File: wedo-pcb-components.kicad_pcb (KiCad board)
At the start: 2 copper layers, 1 part, among them U1 TPS61032

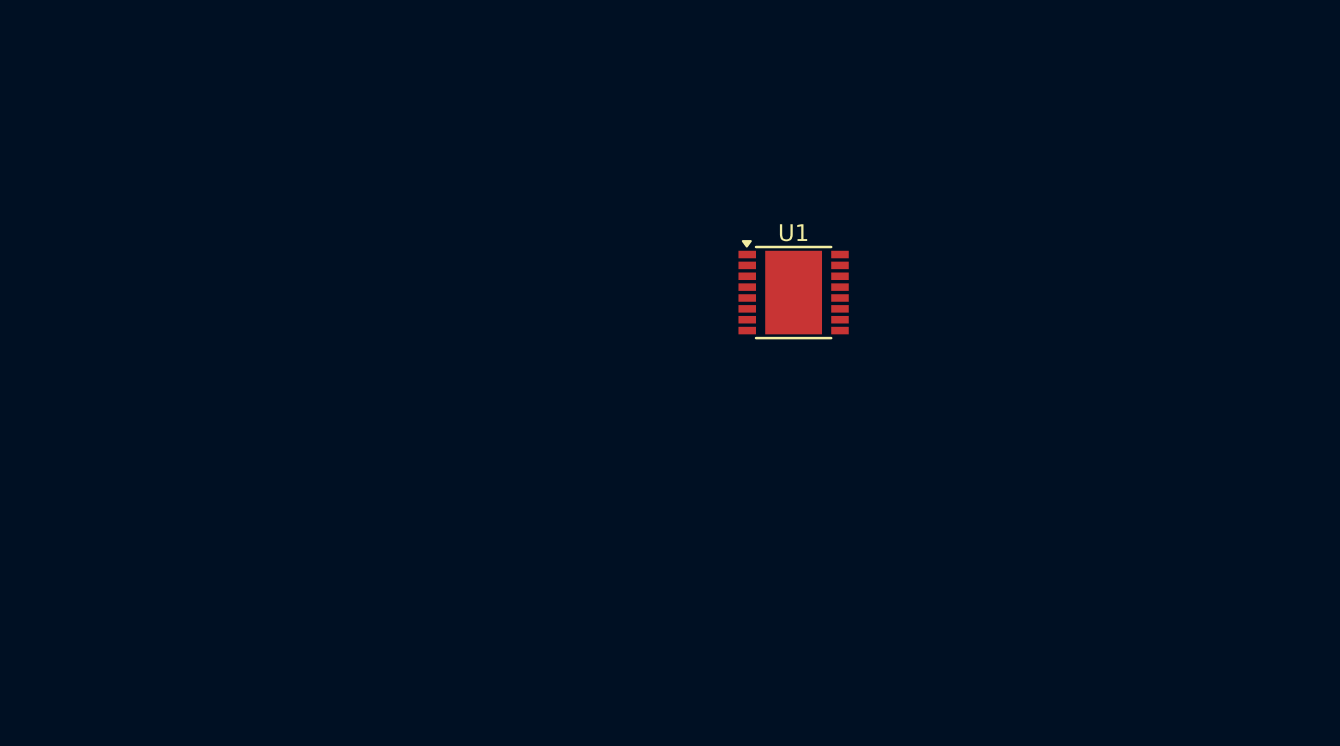
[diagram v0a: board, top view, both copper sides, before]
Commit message: Add 6p6c connector footprint and adjust PCB geometry with mounting holes
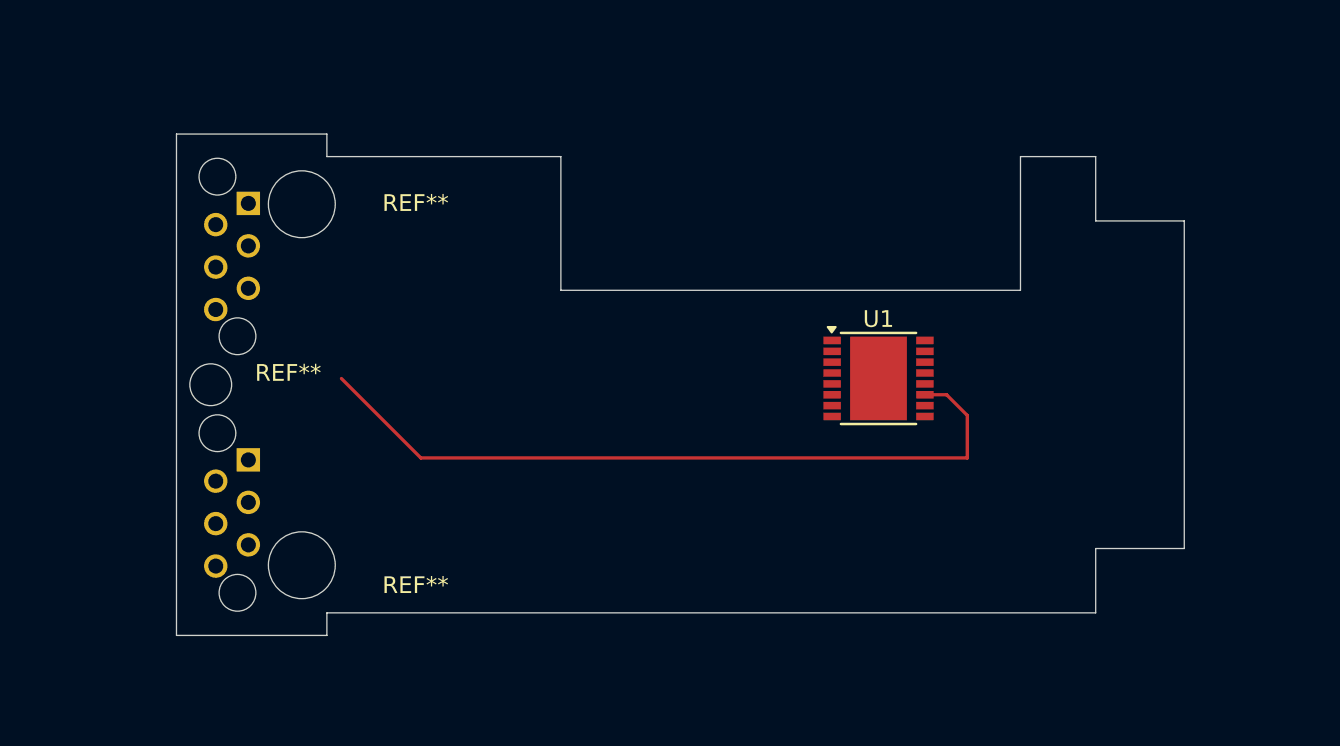
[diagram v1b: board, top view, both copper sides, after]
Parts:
- added J1: 6P6C, Connector_RJ_wedo:RJ12_wedo, B.Cu at (104.3, 119.5)
- added J2: 6P6C, Connector_RJ_wedo:RJ12_wedo, B.Cu at (104.3, 104.2)
- added REF**: MountingHole_2.5mm, MountingHole:MountingHole_2.5mm, F.Cu at (102.0, 115.0)
- added REF**: MountingHole_4mm, MountingHole:MountingHole_4mm, F.Cu at (107.5, 104.2)
- added REF**: MountingHole_4mm, MountingHole:MountingHole_4mm, F.Cu at (107.5, 125.8)
- moved U1 7.23 mm to (142.0, 114.6)
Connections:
- U1 pad 11: unconnected-(U1-GND-Pad11) -> GND
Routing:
- net GND: track 0.00 -> 45.0 mm
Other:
- board outline added: 60.3 x 30 mm

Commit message: Adjusted PCB size, added battery blade connector, also added RGB LED and push button switch
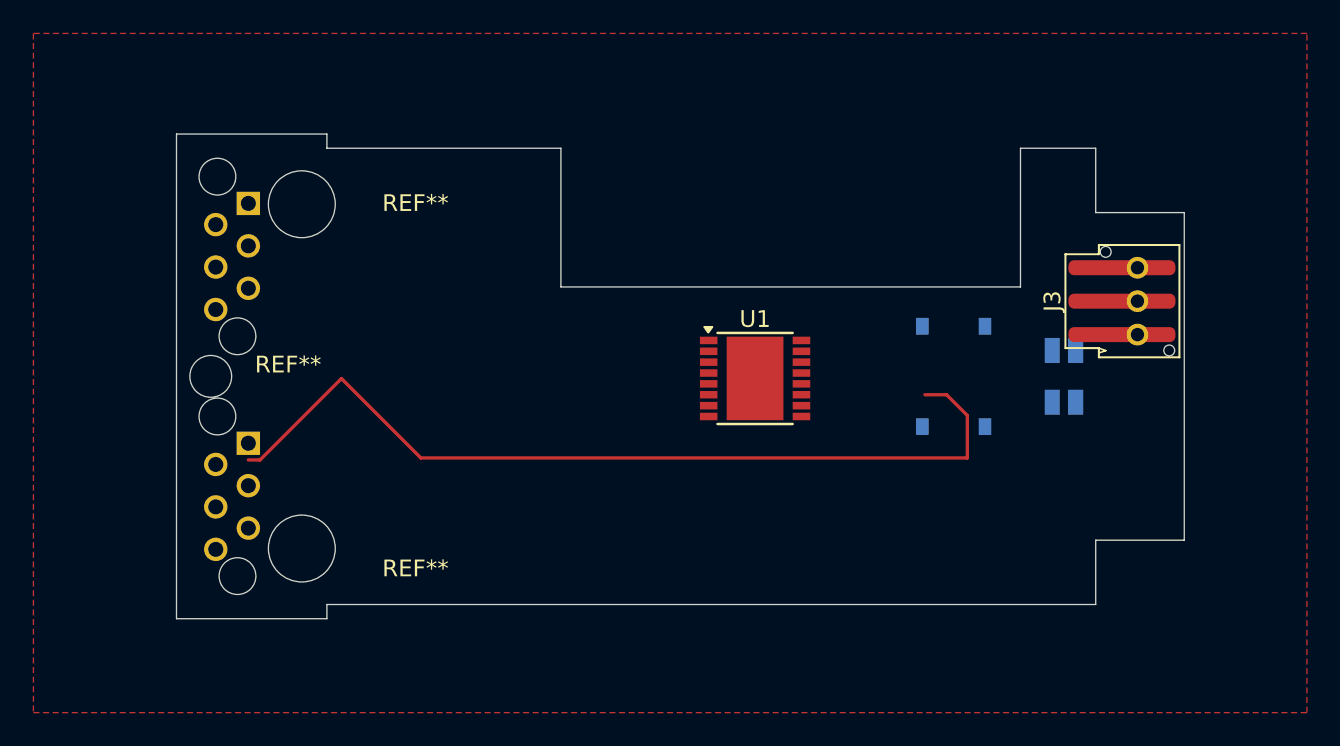
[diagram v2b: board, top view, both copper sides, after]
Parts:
- added D1: LED_RGBK, LED_SMD:LED_RGB_Wuerth-PLCC4_3.2x2.8mm_150141M173100, B.Cu at (153.1, 114.5)
- added J3: Conn_01x03_Pin, Connector_battery_blade:Male_RoundBlade_1x03_P2.0mm_Horizontal, F.Cu at (157.5, 110.0)
- added SW2: SW_Push_Dual_x2, Button_Switch_SMD:SW_Push_1P1T_XKB_TS-1187A, B.Cu at (146.5, 114.5)
- moved U1 7.38 mm to (134.6, 114.6)
- moved J1 1.00 mm to (104.3, 118.5)
- moved REF** 1.00 mm to (107.5, 124.8)
- moved REF** 0.50 mm to (102.0, 114.5)
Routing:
- net GND: track 45.0 -> 52.6 mm
- added copper zone on F.Cu, net GND
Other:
- board size 60.3 x 30 mm -> 60.3 x 29 mm

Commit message: Moved motor/sensor connectors further to edges in Y direction (were too close to center by mistake), updated battery blade connector with two holes to also support THD version, slightly moved battery blade connector towards center in X direction for better clearance
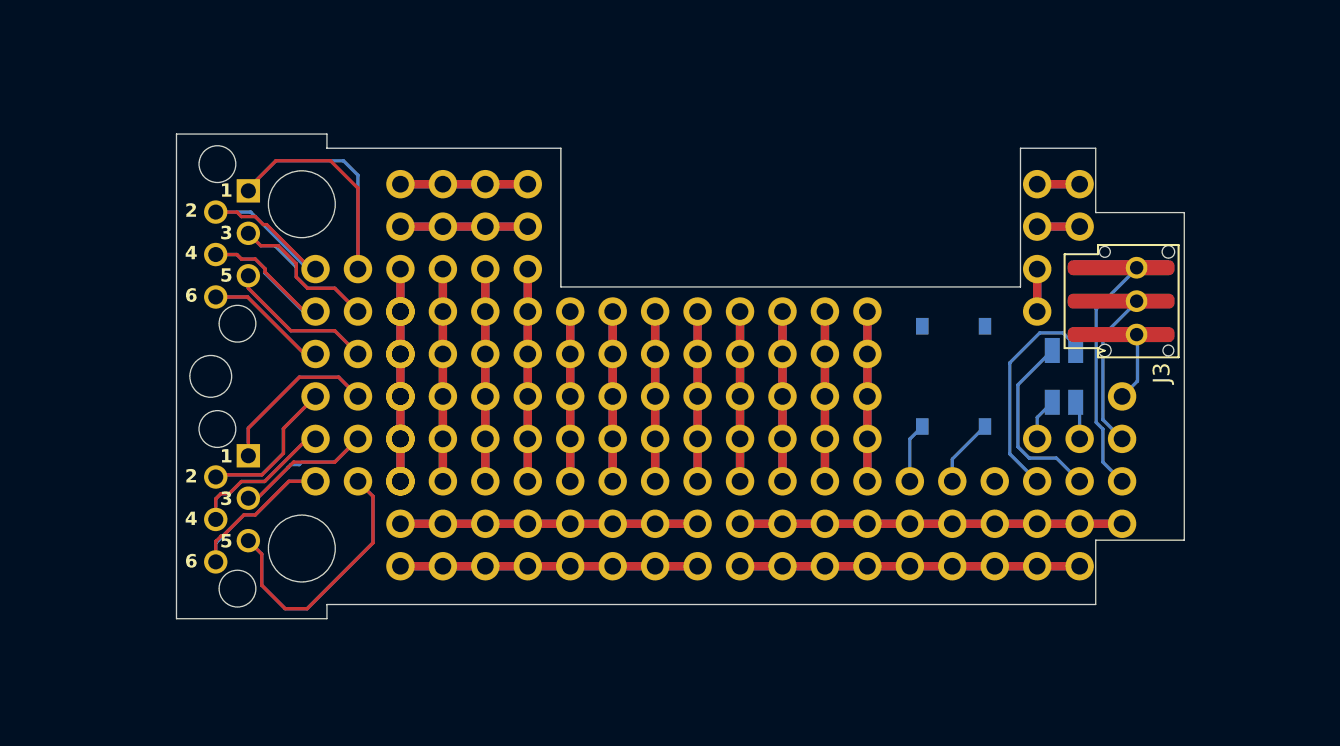
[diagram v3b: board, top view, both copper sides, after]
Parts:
- removed U1: TPS61032, Package_SO:HTSSOP-16-1EP_4.4x5mm_P0.65mm_EP3.4x5mm
- added REF**: Round_Pad_1.7mm_Hole_1.0mm, proto-pcb-pads:RoundPad_1.7mm_Hole_1.0mm, F.Cu at (113.4, 103.0)
- added REF**: Pad_Link_1.7mm_Width_1.0mm, proto-pcb-silks:PadLink_1.7mm_Width_1.0mm, B.Cu at (113.4, 103.0)
- added REF**: Pad_Link_1.7mm_Width_1.0mm, proto-pcb-silks:PadLink_1.7mm_Width_1.0mm, B.Cu at (113.4, 123.3)
- added REF**1: Round_Pad_1.7mm_Hole_1.0mm, proto-pcb-pads:RoundPad_1.7mm_Hole_1.0mm, F.Cu at (115.9, 103.0)
- added REF**10: Pad_Link_1.7mm_Width_1.0mm, proto-pcb-silks:PadLink_1.7mm_Width_1.0mm, B.Cu at (113.4, 125.9)
- added REF**100: Round_Pad_1.7mm_Hole_1.0mm, proto-pcb-pads:RoundPad_1.7mm_Hole_1.0mm, F.Cu at (138.8, 115.7)
- added REF**101: Round_Pad_1.7mm_Hole_1.0mm, proto-pcb-pads:RoundPad_1.7mm_Hole_1.0mm, F.Cu at (141.3, 115.7)
- added REF**102, REF**126: Round_Pad_1.7mm_Hole_1.0mm, proto-pcb-pads:RoundPad_1.7mm_Hole_1.0mm, F.Cu at (113.4, 120.8)
- added REF**103: Round_Pad_1.7mm_Hole_1.0mm, proto-pcb-pads:RoundPad_1.7mm_Hole_1.0mm, F.Cu at (110.9, 120.8)
- added REF**104: Round_Pad_1.7mm_Hole_1.0mm, proto-pcb-pads:RoundPad_1.7mm_Hole_1.0mm, F.Cu at (108.3, 120.8)
- added REF**107: Round_Pad_1.7mm_Hole_1.0mm, proto-pcb-pads:RoundPad_1.7mm_Hole_1.0mm, F.Cu at (156.6, 115.7)
- added REF**108, REF**87: Round_Pad_1.7mm_Hole_1.0mm, proto-pcb-pads:RoundPad_1.7mm_Hole_1.0mm, F.Cu at (113.4, 118.2)
- added REF**109: Round_Pad_1.7mm_Hole_1.0mm, proto-pcb-pads:RoundPad_1.7mm_Hole_1.0mm, F.Cu at (115.9, 118.2)
- added REF**11: Pad_Link_1.7mm_Width_1.0mm, proto-pcb-silks:PadLink_1.7mm_Width_1.0mm, B.Cu at (115.9, 125.9)
- added REF**110: Round_Pad_1.7mm_Hole_1.0mm, proto-pcb-pads:RoundPad_1.7mm_Hole_1.0mm, F.Cu at (118.5, 118.2)
- added REF**111: Round_Pad_1.7mm_Hole_1.0mm, proto-pcb-pads:RoundPad_1.7mm_Hole_1.0mm, F.Cu at (121.0, 118.2)
- added REF**112: Round_Pad_1.7mm_Hole_1.0mm, proto-pcb-pads:RoundPad_1.7mm_Hole_1.0mm, F.Cu at (123.6, 118.2)
- added REF**113: Round_Pad_1.7mm_Hole_1.0mm, proto-pcb-pads:RoundPad_1.7mm_Hole_1.0mm, F.Cu at (126.1, 118.2)
- added REF**114: Round_Pad_1.7mm_Hole_1.0mm, proto-pcb-pads:RoundPad_1.7mm_Hole_1.0mm, F.Cu at (128.6, 118.2)
- added REF**115: Round_Pad_1.7mm_Hole_1.0mm, proto-pcb-pads:RoundPad_1.7mm_Hole_1.0mm, F.Cu at (131.2, 118.2)
- added REF**116: Round_Pad_1.7mm_Hole_1.0mm, proto-pcb-pads:RoundPad_1.7mm_Hole_1.0mm, F.Cu at (133.7, 118.2)
- added REF**117: Round_Pad_1.7mm_Hole_1.0mm, proto-pcb-pads:RoundPad_1.7mm_Hole_1.0mm, F.Cu at (136.3, 118.2)
- added REF**118: Round_Pad_1.7mm_Hole_1.0mm, proto-pcb-pads:RoundPad_1.7mm_Hole_1.0mm, F.Cu at (138.8, 118.2)
- added REF**119: Round_Pad_1.7mm_Hole_1.0mm, proto-pcb-pads:RoundPad_1.7mm_Hole_1.0mm, F.Cu at (141.3, 118.2)
- added REF**12: Pad_Link_1.7mm_Width_1.0mm, proto-pcb-silks:PadLink_1.7mm_Width_1.0mm, B.Cu at (118.5, 125.9)
- added REF**123: Round_Pad_1.7mm_Hole_1.0mm, proto-pcb-pads:RoundPad_1.7mm_Hole_1.0mm, F.Cu at (151.5, 118.2)
- added REF**124: Round_Pad_1.7mm_Hole_1.0mm, proto-pcb-pads:RoundPad_1.7mm_Hole_1.0mm, F.Cu at (154.0, 118.2)
- added REF**125: Round_Pad_1.7mm_Hole_1.0mm, proto-pcb-pads:RoundPad_1.7mm_Hole_1.0mm, F.Cu at (156.6, 118.2)
- added REF**127: Round_Pad_1.7mm_Hole_1.0mm, proto-pcb-pads:RoundPad_1.7mm_Hole_1.0mm, F.Cu at (115.9, 120.8)
- added REF**128: Round_Pad_1.7mm_Hole_1.0mm, proto-pcb-pads:RoundPad_1.7mm_Hole_1.0mm, F.Cu at (118.5, 120.8)
- added REF**129: Round_Pad_1.7mm_Hole_1.0mm, proto-pcb-pads:RoundPad_1.7mm_Hole_1.0mm, F.Cu at (121.0, 120.8)
- added REF**13: Pad_Link_1.7mm_Width_1.0mm, proto-pcb-silks:PadLink_1.7mm_Width_1.0mm, B.Cu at (121.0, 125.9)
- added REF**130: Round_Pad_1.7mm_Hole_1.0mm, proto-pcb-pads:RoundPad_1.7mm_Hole_1.0mm, F.Cu at (123.6, 120.8)
- added REF**131: Round_Pad_1.7mm_Hole_1.0mm, proto-pcb-pads:RoundPad_1.7mm_Hole_1.0mm, F.Cu at (126.1, 120.8)
- added REF**132: Round_Pad_1.7mm_Hole_1.0mm, proto-pcb-pads:RoundPad_1.7mm_Hole_1.0mm, F.Cu at (128.6, 120.8)
- added REF**133: Round_Pad_1.7mm_Hole_1.0mm, proto-pcb-pads:RoundPad_1.7mm_Hole_1.0mm, F.Cu at (131.2, 120.8)
- added REF**134: Round_Pad_1.7mm_Hole_1.0mm, proto-pcb-pads:RoundPad_1.7mm_Hole_1.0mm, F.Cu at (133.7, 120.8)
- added REF**135: Round_Pad_1.7mm_Hole_1.0mm, proto-pcb-pads:RoundPad_1.7mm_Hole_1.0mm, F.Cu at (136.3, 120.8)
- added REF**136: Round_Pad_1.7mm_Hole_1.0mm, proto-pcb-pads:RoundPad_1.7mm_Hole_1.0mm, F.Cu at (138.8, 120.8)
- added REF**137: Round_Pad_1.7mm_Hole_1.0mm, proto-pcb-pads:RoundPad_1.7mm_Hole_1.0mm, F.Cu at (141.3, 120.8)
- added REF**138: Round_Pad_1.7mm_Hole_1.0mm, proto-pcb-pads:RoundPad_1.7mm_Hole_1.0mm, F.Cu at (143.9, 120.8)
- added REF**139: Round_Pad_1.7mm_Hole_1.0mm, proto-pcb-pads:RoundPad_1.7mm_Hole_1.0mm, F.Cu at (146.4, 120.8)
- added REF**14: Pad_Link_1.7mm_Width_1.0mm, proto-pcb-silks:PadLink_1.7mm_Width_1.0mm, B.Cu at (123.6, 125.9)
- added REF**140: Round_Pad_1.7mm_Hole_1.0mm, proto-pcb-pads:RoundPad_1.7mm_Hole_1.0mm, F.Cu at (149.0, 120.8)
- added REF**141: Round_Pad_1.7mm_Hole_1.0mm, proto-pcb-pads:RoundPad_1.7mm_Hole_1.0mm, F.Cu at (151.5, 120.8)
- added REF**142: Round_Pad_1.7mm_Hole_1.0mm, proto-pcb-pads:RoundPad_1.7mm_Hole_1.0mm, F.Cu at (154.0, 120.8)
- added REF**143: Round_Pad_1.7mm_Hole_1.0mm, proto-pcb-pads:RoundPad_1.7mm_Hole_1.0mm, F.Cu at (156.6, 120.8)
- added REF**144: Round_Pad_1.7mm_Hole_1.0mm, proto-pcb-pads:RoundPad_1.7mm_Hole_1.0mm, F.Cu at (113.4, 123.3)
- added REF**145: Round_Pad_1.7mm_Hole_1.0mm, proto-pcb-pads:RoundPad_1.7mm_Hole_1.0mm, F.Cu at (115.9, 123.3)
- added REF**146: Round_Pad_1.7mm_Hole_1.0mm, proto-pcb-pads:RoundPad_1.7mm_Hole_1.0mm, F.Cu at (118.5, 123.3)
- added REF**147: Round_Pad_1.7mm_Hole_1.0mm, proto-pcb-pads:RoundPad_1.7mm_Hole_1.0mm, F.Cu at (121.0, 123.3)
- added REF**148: Round_Pad_1.7mm_Hole_1.0mm, proto-pcb-pads:RoundPad_1.7mm_Hole_1.0mm, F.Cu at (123.6, 123.3)
- added REF**149: Round_Pad_1.7mm_Hole_1.0mm, proto-pcb-pads:RoundPad_1.7mm_Hole_1.0mm, F.Cu at (126.1, 123.3)
- added REF**15: Round_Pad_1.7mm_Hole_1.0mm, proto-pcb-pads:RoundPad_1.7mm_Hole_1.0mm, F.Cu at (151.5, 103.0)
- added REF**150: Round_Pad_1.7mm_Hole_1.0mm, proto-pcb-pads:RoundPad_1.7mm_Hole_1.0mm, F.Cu at (128.6, 123.3)
- added REF**151: Round_Pad_1.7mm_Hole_1.0mm, proto-pcb-pads:RoundPad_1.7mm_Hole_1.0mm, F.Cu at (131.2, 123.3)
- added REF**152: Round_Pad_1.7mm_Hole_1.0mm, proto-pcb-pads:RoundPad_1.7mm_Hole_1.0mm, F.Cu at (133.7, 123.3)
- added REF**153: Round_Pad_1.7mm_Hole_1.0mm, proto-pcb-pads:RoundPad_1.7mm_Hole_1.0mm, F.Cu at (136.3, 123.3)
- added REF**154: Round_Pad_1.7mm_Hole_1.0mm, proto-pcb-pads:RoundPad_1.7mm_Hole_1.0mm, F.Cu at (138.8, 123.3)
- added REF**155: Round_Pad_1.7mm_Hole_1.0mm, proto-pcb-pads:RoundPad_1.7mm_Hole_1.0mm, F.Cu at (141.3, 123.3)
- added REF**156: Round_Pad_1.7mm_Hole_1.0mm, proto-pcb-pads:RoundPad_1.7mm_Hole_1.0mm, F.Cu at (143.9, 123.3)
- added REF**157: Round_Pad_1.7mm_Hole_1.0mm, proto-pcb-pads:RoundPad_1.7mm_Hole_1.0mm, F.Cu at (146.4, 123.3)
- added REF**158: Round_Pad_1.7mm_Hole_1.0mm, proto-pcb-pads:RoundPad_1.7mm_Hole_1.0mm, F.Cu at (149.0, 123.3)
- added REF**159: Round_Pad_1.7mm_Hole_1.0mm, proto-pcb-pads:RoundPad_1.7mm_Hole_1.0mm, F.Cu at (151.5, 123.3)
- added REF**16: Round_Pad_1.7mm_Hole_1.0mm, proto-pcb-pads:RoundPad_1.7mm_Hole_1.0mm, F.Cu at (154.0, 103.0)
- added REF**160: Round_Pad_1.7mm_Hole_1.0mm, proto-pcb-pads:RoundPad_1.7mm_Hole_1.0mm, F.Cu at (154.0, 123.3)
- added REF**161: Round_Pad_1.7mm_Hole_1.0mm, proto-pcb-pads:RoundPad_1.7mm_Hole_1.0mm, F.Cu at (156.6, 123.3)
- added REF**162: Round_Pad_1.7mm_Hole_1.0mm, proto-pcb-pads:RoundPad_1.7mm_Hole_1.0mm, F.Cu at (113.4, 125.9)
- added REF**163: Round_Pad_1.7mm_Hole_1.0mm, proto-pcb-pads:RoundPad_1.7mm_Hole_1.0mm, F.Cu at (115.9, 125.9)
- added REF**164: Round_Pad_1.7mm_Hole_1.0mm, proto-pcb-pads:RoundPad_1.7mm_Hole_1.0mm, F.Cu at (118.5, 125.9)
- added REF**165: Round_Pad_1.7mm_Hole_1.0mm, proto-pcb-pads:RoundPad_1.7mm_Hole_1.0mm, F.Cu at (121.0, 125.9)
- added REF**166: Round_Pad_1.7mm_Hole_1.0mm, proto-pcb-pads:RoundPad_1.7mm_Hole_1.0mm, F.Cu at (123.6, 125.9)
- added REF**167: Round_Pad_1.7mm_Hole_1.0mm, proto-pcb-pads:RoundPad_1.7mm_Hole_1.0mm, F.Cu at (126.1, 125.9)
- added REF**168: Round_Pad_1.7mm_Hole_1.0mm, proto-pcb-pads:RoundPad_1.7mm_Hole_1.0mm, F.Cu at (128.6, 125.9)
- added REF**169: Round_Pad_1.7mm_Hole_1.0mm, proto-pcb-pads:RoundPad_1.7mm_Hole_1.0mm, F.Cu at (131.2, 125.9)
- added REF**17: Pad_Link_1.7mm_Width_1.0mm, proto-pcb-silks:PadLink_1.7mm_Width_1.0mm, B.Cu at (126.1, 125.9)
- added REF**170: Round_Pad_1.7mm_Hole_1.0mm, proto-pcb-pads:RoundPad_1.7mm_Hole_1.0mm, F.Cu at (133.7, 125.9)
- added REF**171: Round_Pad_1.7mm_Hole_1.0mm, proto-pcb-pads:RoundPad_1.7mm_Hole_1.0mm, F.Cu at (136.3, 125.9)
- added REF**172: Round_Pad_1.7mm_Hole_1.0mm, proto-pcb-pads:RoundPad_1.7mm_Hole_1.0mm, F.Cu at (138.8, 125.9)
- added REF**173: Round_Pad_1.7mm_Hole_1.0mm, proto-pcb-pads:RoundPad_1.7mm_Hole_1.0mm, F.Cu at (141.3, 125.9)
- added REF**174: Round_Pad_1.7mm_Hole_1.0mm, proto-pcb-pads:RoundPad_1.7mm_Hole_1.0mm, F.Cu at (143.9, 125.9)
- added REF**175: Round_Pad_1.7mm_Hole_1.0mm, proto-pcb-pads:RoundPad_1.7mm_Hole_1.0mm, F.Cu at (146.4, 125.9)
- added REF**176: Round_Pad_1.7mm_Hole_1.0mm, proto-pcb-pads:RoundPad_1.7mm_Hole_1.0mm, F.Cu at (149.0, 125.9)
- added REF**177: Round_Pad_1.7mm_Hole_1.0mm, proto-pcb-pads:RoundPad_1.7mm_Hole_1.0mm, F.Cu at (151.5, 125.9)
- added REF**178: Round_Pad_1.7mm_Hole_1.0mm, proto-pcb-pads:RoundPad_1.7mm_Hole_1.0mm, F.Cu at (154.0, 125.9)
- added REF**18: Round_Pad_1.7mm_Hole_1.0mm, proto-pcb-pads:RoundPad_1.7mm_Hole_1.0mm, F.Cu at (113.4, 105.5)
- added REF**183: Pad_Link_1.7mm_Width_1.0mm, proto-pcb-silks:PadLink_1.7mm_Width_1.0mm, B.Cu at (151.5, 103.0)
- added REF**187: Pad_Link_1.7mm_Width_1.0mm, proto-pcb-silks:PadLink_1.7mm_Width_1.0mm, B.Cu at (113.4, 105.5)
- added REF**188: Pad_Link_1.7mm_Width_1.0mm, proto-pcb-silks:PadLink_1.7mm_Width_1.0mm, B.Cu at (115.9, 105.5)
- added REF**189: Pad_Link_1.7mm_Width_1.0mm, proto-pcb-silks:PadLink_1.7mm_Width_1.0mm, B.Cu at (118.5, 105.5)
- added REF**19: Round_Pad_1.7mm_Hole_1.0mm, proto-pcb-pads:RoundPad_1.7mm_Hole_1.0mm, F.Cu at (115.9, 105.5)
- added REF**2: Round_Pad_1.7mm_Hole_1.0mm, proto-pcb-pads:RoundPad_1.7mm_Hole_1.0mm, F.Cu at (118.5, 103.0)
- added REF**20: Round_Pad_1.7mm_Hole_1.0mm, proto-pcb-pads:RoundPad_1.7mm_Hole_1.0mm, F.Cu at (118.5, 105.5)
- added REF**202: Pad_Link_1.7mm_Width_1.0mm, proto-pcb-silks:PadLink_1.7mm_Width_1.0mm, B.Cu at (113.4, 108.1)
- added REF**202: Pad_Link_1.7mm_Width_1.0mm, proto-pcb-silks:PadLink_1.7mm_Width_1.0mm, B.Cu at (151.5, 105.5)
- added REF**202: Pad_Link_1.7mm_Width_1.0mm, proto-pcb-silks:PadLink_1.7mm_Width_1.0mm, B.Cu at (151.5, 108.1)
- added REF**203: Pad_Link_1.7mm_Width_1.0mm, proto-pcb-silks:PadLink_1.7mm_Width_1.0mm, B.Cu at (115.9, 108.1)
- added REF**204: Pad_Link_1.7mm_Width_1.0mm, proto-pcb-silks:PadLink_1.7mm_Width_1.0mm, B.Cu at (118.5, 108.1)
- added REF**205: Pad_Link_1.7mm_Width_1.0mm, proto-pcb-silks:PadLink_1.7mm_Width_1.0mm, B.Cu at (121.0, 108.1)
- added REF**21: Round_Pad_1.7mm_Hole_1.0mm, proto-pcb-pads:RoundPad_1.7mm_Hole_1.0mm, F.Cu at (121.0, 105.5)
- added REF**214: Pad_Link_1.7mm_Width_1.0mm, proto-pcb-silks:PadLink_1.7mm_Width_1.0mm, B.Cu at (113.4, 110.6)
- added REF**215: Pad_Link_1.7mm_Width_1.0mm, proto-pcb-silks:PadLink_1.7mm_Width_1.0mm, B.Cu at (115.9, 110.6)
- added REF**216: Pad_Link_1.7mm_Width_1.0mm, proto-pcb-silks:PadLink_1.7mm_Width_1.0mm, B.Cu at (118.5, 110.6)
- added REF**217: Pad_Link_1.7mm_Width_1.0mm, proto-pcb-silks:PadLink_1.7mm_Width_1.0mm, B.Cu at (121.0, 110.6)
- added REF**218: Pad_Link_1.7mm_Width_1.0mm, proto-pcb-silks:PadLink_1.7mm_Width_1.0mm, B.Cu at (123.6, 110.6)
- added REF**219: Pad_Link_1.7mm_Width_1.0mm, proto-pcb-silks:PadLink_1.7mm_Width_1.0mm, B.Cu at (126.1, 110.6)
- added REF**22: Pad_Link_1.7mm_Width_1.0mm, proto-pcb-silks:PadLink_1.7mm_Width_1.0mm, B.Cu at (128.6, 125.9)
- added REF**220: Pad_Link_1.7mm_Width_1.0mm, proto-pcb-silks:PadLink_1.7mm_Width_1.0mm, B.Cu at (128.6, 110.6)
- added REF**221: Pad_Link_1.7mm_Width_1.0mm, proto-pcb-silks:PadLink_1.7mm_Width_1.0mm, B.Cu at (131.2, 110.6)
- added REF**222: Pad_Link_1.7mm_Width_1.0mm, proto-pcb-silks:PadLink_1.7mm_Width_1.0mm, B.Cu at (133.7, 110.6)
- added REF**223: Pad_Link_1.7mm_Width_1.0mm, proto-pcb-silks:PadLink_1.7mm_Width_1.0mm, B.Cu at (136.3, 110.6)
- added REF**224: Pad_Link_1.7mm_Width_1.0mm, proto-pcb-silks:PadLink_1.7mm_Width_1.0mm, B.Cu at (138.8, 110.6)
- added REF**225: Pad_Link_1.7mm_Width_1.0mm, proto-pcb-silks:PadLink_1.7mm_Width_1.0mm, B.Cu at (141.3, 110.6)
- added REF**226: Pad_Link_1.7mm_Width_1.0mm, proto-pcb-silks:PadLink_1.7mm_Width_1.0mm, B.Cu at (113.4, 113.2)
- added REF**227: Pad_Link_1.7mm_Width_1.0mm, proto-pcb-silks:PadLink_1.7mm_Width_1.0mm, B.Cu at (115.9, 113.2)
- added REF**228: Pad_Link_1.7mm_Width_1.0mm, proto-pcb-silks:PadLink_1.7mm_Width_1.0mm, B.Cu at (118.5, 113.2)
- added REF**229: Pad_Link_1.7mm_Width_1.0mm, proto-pcb-silks:PadLink_1.7mm_Width_1.0mm, B.Cu at (121.0, 113.2)
- added REF**23: Pad_Link_1.7mm_Width_1.0mm, proto-pcb-silks:PadLink_1.7mm_Width_1.0mm, B.Cu at (136.3, 123.3)
- added REF**230: Pad_Link_1.7mm_Width_1.0mm, proto-pcb-silks:PadLink_1.7mm_Width_1.0mm, B.Cu at (123.6, 113.2)
- added REF**231: Pad_Link_1.7mm_Width_1.0mm, proto-pcb-silks:PadLink_1.7mm_Width_1.0mm, B.Cu at (126.1, 113.2)
- added REF**232: Pad_Link_1.7mm_Width_1.0mm, proto-pcb-silks:PadLink_1.7mm_Width_1.0mm, B.Cu at (128.6, 113.2)
- added REF**233: Pad_Link_1.7mm_Width_1.0mm, proto-pcb-silks:PadLink_1.7mm_Width_1.0mm, B.Cu at (131.2, 113.2)
- added REF**234: Pad_Link_1.7mm_Width_1.0mm, proto-pcb-silks:PadLink_1.7mm_Width_1.0mm, B.Cu at (133.7, 113.2)
- added REF**235: Pad_Link_1.7mm_Width_1.0mm, proto-pcb-silks:PadLink_1.7mm_Width_1.0mm, B.Cu at (136.3, 113.2)
- added REF**236: Pad_Link_1.7mm_Width_1.0mm, proto-pcb-silks:PadLink_1.7mm_Width_1.0mm, B.Cu at (138.8, 113.2)
- added REF**237: Pad_Link_1.7mm_Width_1.0mm, proto-pcb-silks:PadLink_1.7mm_Width_1.0mm, B.Cu at (141.3, 113.2)
- added REF**238: Pad_Link_1.7mm_Width_1.0mm, proto-pcb-silks:PadLink_1.7mm_Width_1.0mm, B.Cu at (113.4, 115.7)
- added REF**239: Pad_Link_1.7mm_Width_1.0mm, proto-pcb-silks:PadLink_1.7mm_Width_1.0mm, B.Cu at (115.9, 115.7)
- added REF**24: Pad_Link_1.7mm_Width_1.0mm, proto-pcb-silks:PadLink_1.7mm_Width_1.0mm, B.Cu at (138.8, 123.3)
- added REF**240: Pad_Link_1.7mm_Width_1.0mm, proto-pcb-silks:PadLink_1.7mm_Width_1.0mm, B.Cu at (118.5, 115.7)
- added REF**241: Pad_Link_1.7mm_Width_1.0mm, proto-pcb-silks:PadLink_1.7mm_Width_1.0mm, B.Cu at (121.0, 115.7)
- added REF**242: Pad_Link_1.7mm_Width_1.0mm, proto-pcb-silks:PadLink_1.7mm_Width_1.0mm, B.Cu at (123.6, 115.7)
- added REF**243: Pad_Link_1.7mm_Width_1.0mm, proto-pcb-silks:PadLink_1.7mm_Width_1.0mm, B.Cu at (126.1, 115.7)
- added REF**244: Pad_Link_1.7mm_Width_1.0mm, proto-pcb-silks:PadLink_1.7mm_Width_1.0mm, B.Cu at (128.6, 115.7)
- added REF**245: Pad_Link_1.7mm_Width_1.0mm, proto-pcb-silks:PadLink_1.7mm_Width_1.0mm, B.Cu at (131.2, 115.7)
- added REF**246: Pad_Link_1.7mm_Width_1.0mm, proto-pcb-silks:PadLink_1.7mm_Width_1.0mm, B.Cu at (133.7, 115.7)
- added REF**247: Pad_Link_1.7mm_Width_1.0mm, proto-pcb-silks:PadLink_1.7mm_Width_1.0mm, B.Cu at (136.3, 115.7)
- added REF**248: Pad_Link_1.7mm_Width_1.0mm, proto-pcb-silks:PadLink_1.7mm_Width_1.0mm, B.Cu at (138.8, 115.7)
- added REF**249: Pad_Link_1.7mm_Width_1.0mm, proto-pcb-silks:PadLink_1.7mm_Width_1.0mm, B.Cu at (141.3, 115.7)
- added REF**25: Pad_Link_1.7mm_Width_1.0mm, proto-pcb-silks:PadLink_1.7mm_Width_1.0mm, B.Cu at (141.3, 123.3)
- added REF**250: Pad_Link_1.7mm_Width_1.0mm, proto-pcb-silks:PadLink_1.7mm_Width_1.0mm, B.Cu at (113.4, 118.2)
- added REF**251: Pad_Link_1.7mm_Width_1.0mm, proto-pcb-silks:PadLink_1.7mm_Width_1.0mm, B.Cu at (115.9, 118.2)
- added REF**252: Pad_Link_1.7mm_Width_1.0mm, proto-pcb-silks:PadLink_1.7mm_Width_1.0mm, B.Cu at (118.5, 118.2)
- added REF**253: Pad_Link_1.7mm_Width_1.0mm, proto-pcb-silks:PadLink_1.7mm_Width_1.0mm, B.Cu at (121.0, 118.2)
- added REF**254: Pad_Link_1.7mm_Width_1.0mm, proto-pcb-silks:PadLink_1.7mm_Width_1.0mm, B.Cu at (123.6, 118.2)
- added REF**255: Pad_Link_1.7mm_Width_1.0mm, proto-pcb-silks:PadLink_1.7mm_Width_1.0mm, B.Cu at (126.1, 118.2)
- added REF**256: Pad_Link_1.7mm_Width_1.0mm, proto-pcb-silks:PadLink_1.7mm_Width_1.0mm, B.Cu at (128.6, 118.2)
- added REF**257: Pad_Link_1.7mm_Width_1.0mm, proto-pcb-silks:PadLink_1.7mm_Width_1.0mm, B.Cu at (131.2, 118.2)
- added REF**258: Pad_Link_1.7mm_Width_1.0mm, proto-pcb-silks:PadLink_1.7mm_Width_1.0mm, B.Cu at (133.7, 118.2)
- added REF**259: Pad_Link_1.7mm_Width_1.0mm, proto-pcb-silks:PadLink_1.7mm_Width_1.0mm, B.Cu at (136.3, 118.2)
- added REF**26: Pad_Link_1.7mm_Width_1.0mm, proto-pcb-silks:PadLink_1.7mm_Width_1.0mm, B.Cu at (143.9, 123.3)
- added REF**260: Pad_Link_1.7mm_Width_1.0mm, proto-pcb-silks:PadLink_1.7mm_Width_1.0mm, B.Cu at (138.8, 118.2)
- added REF**261: Pad_Link_1.7mm_Width_1.0mm, proto-pcb-silks:PadLink_1.7mm_Width_1.0mm, B.Cu at (141.3, 118.2)
- added REF**27: Pad_Link_1.7mm_Width_1.0mm, proto-pcb-silks:PadLink_1.7mm_Width_1.0mm, B.Cu at (146.4, 123.3)
- added REF**28: Pad_Link_1.7mm_Width_1.0mm, proto-pcb-silks:PadLink_1.7mm_Width_1.0mm, B.Cu at (149.0, 123.3)
- added REF**29: Pad_Link_1.7mm_Width_1.0mm, proto-pcb-silks:PadLink_1.7mm_Width_1.0mm, B.Cu at (151.5, 123.3)
- added REF**3: Round_Pad_1.7mm_Hole_1.0mm, proto-pcb-pads:RoundPad_1.7mm_Hole_1.0mm, F.Cu at (121.0, 103.0)
- added REF**30: Pad_Link_1.7mm_Width_1.0mm, proto-pcb-silks:PadLink_1.7mm_Width_1.0mm, B.Cu at (154.0, 123.3)
- added REF**31: Pad_Link_1.7mm_Width_1.0mm, proto-pcb-silks:PadLink_1.7mm_Width_1.0mm, B.Cu at (133.7, 125.9)
- added REF**32: Pad_Link_1.7mm_Width_1.0mm, proto-pcb-silks:PadLink_1.7mm_Width_1.0mm, B.Cu at (136.3, 125.9)
- added REF**33: Round_Pad_1.7mm_Hole_1.0mm, proto-pcb-pads:RoundPad_1.7mm_Hole_1.0mm, F.Cu at (151.5, 105.5)
- added REF**34: Round_Pad_1.7mm_Hole_1.0mm, proto-pcb-pads:RoundPad_1.7mm_Hole_1.0mm, F.Cu at (154.0, 105.5)
- added REF**35: Pad_Link_1.7mm_Width_1.0mm, proto-pcb-silks:PadLink_1.7mm_Width_1.0mm, B.Cu at (138.8, 125.9)
- added REF**36: Round_Pad_1.7mm_Hole_1.0mm, proto-pcb-pads:RoundPad_1.7mm_Hole_1.0mm, F.Cu at (113.4, 108.1)
- added REF**37: Round_Pad_1.7mm_Hole_1.0mm, proto-pcb-pads:RoundPad_1.7mm_Hole_1.0mm, F.Cu at (115.9, 108.1)
- added REF**38: Round_Pad_1.7mm_Hole_1.0mm, proto-pcb-pads:RoundPad_1.7mm_Hole_1.0mm, F.Cu at (118.5, 108.1)
- added REF**39: Round_Pad_1.7mm_Hole_1.0mm, proto-pcb-pads:RoundPad_1.7mm_Hole_1.0mm, F.Cu at (121.0, 108.1)
- added REF**4: Pad_Link_1.7mm_Width_1.0mm, proto-pcb-silks:PadLink_1.7mm_Width_1.0mm, B.Cu at (115.9, 123.3)
- added REF**40: Round_Pad_1.7mm_Hole_1.0mm, proto-pcb-pads:RoundPad_1.7mm_Hole_1.0mm, F.Cu at (110.9, 108.1)
- added REF**41: Pad_Link_1.7mm_Width_1.0mm, proto-pcb-silks:PadLink_1.7mm_Width_1.0mm, B.Cu at (141.3, 125.9)
- added REF**42: Pad_Link_1.7mm_Width_1.0mm, proto-pcb-silks:PadLink_1.7mm_Width_1.0mm, B.Cu at (143.9, 125.9)
- added REF**43: Pad_Link_1.7mm_Width_1.0mm, proto-pcb-silks:PadLink_1.7mm_Width_1.0mm, B.Cu at (146.4, 125.9)
- added REF**44: Pad_Link_1.7mm_Width_1.0mm, proto-pcb-silks:PadLink_1.7mm_Width_1.0mm, B.Cu at (149.0, 125.9)
- added REF**45: Pad_Link_1.7mm_Width_1.0mm, proto-pcb-silks:PadLink_1.7mm_Width_1.0mm, B.Cu at (151.5, 125.9)
- added REF**46: Pad_Link_1.7mm_Width_1.0mm, proto-pcb-silks:PadLink_1.7mm_Width_1.0mm, B.Cu at (115.9, 103.0)
- added REF**47: Pad_Link_1.7mm_Width_1.0mm, proto-pcb-silks:PadLink_1.7mm_Width_1.0mm, B.Cu at (118.5, 103.0)
- added REF**5: Pad_Link_1.7mm_Width_1.0mm, proto-pcb-silks:PadLink_1.7mm_Width_1.0mm, B.Cu at (118.5, 123.3)
- added REF**51: Round_Pad_1.7mm_Hole_1.0mm, proto-pcb-pads:RoundPad_1.7mm_Hole_1.0mm, F.Cu at (151.5, 108.1)
- added REF**52: Round_Pad_1.7mm_Hole_1.0mm, proto-pcb-pads:RoundPad_1.7mm_Hole_1.0mm, F.Cu at (108.3, 108.1)
- added REF**53, REF**54: Round_Pad_1.7mm_Hole_1.0mm, proto-pcb-pads:RoundPad_1.7mm_Hole_1.0mm, F.Cu at (113.4, 110.6)
- added REF**55: Round_Pad_1.7mm_Hole_1.0mm, proto-pcb-pads:RoundPad_1.7mm_Hole_1.0mm, F.Cu at (115.9, 110.6)
- added REF**56: Round_Pad_1.7mm_Hole_1.0mm, proto-pcb-pads:RoundPad_1.7mm_Hole_1.0mm, F.Cu at (118.5, 110.6)
- added REF**57: Round_Pad_1.7mm_Hole_1.0mm, proto-pcb-pads:RoundPad_1.7mm_Hole_1.0mm, F.Cu at (121.0, 110.6)
- added REF**58: Round_Pad_1.7mm_Hole_1.0mm, proto-pcb-pads:RoundPad_1.7mm_Hole_1.0mm, F.Cu at (123.6, 110.6)
- added REF**59: Round_Pad_1.7mm_Hole_1.0mm, proto-pcb-pads:RoundPad_1.7mm_Hole_1.0mm, F.Cu at (126.1, 110.6)
- added REF**6: Pad_Link_1.7mm_Width_1.0mm, proto-pcb-silks:PadLink_1.7mm_Width_1.0mm, B.Cu at (121.0, 123.3)
- added REF**60: Round_Pad_1.7mm_Hole_1.0mm, proto-pcb-pads:RoundPad_1.7mm_Hole_1.0mm, F.Cu at (128.6, 110.6)
- added REF**61: Round_Pad_1.7mm_Hole_1.0mm, proto-pcb-pads:RoundPad_1.7mm_Hole_1.0mm, F.Cu at (131.2, 110.6)
- added REF**62: Round_Pad_1.7mm_Hole_1.0mm, proto-pcb-pads:RoundPad_1.7mm_Hole_1.0mm, F.Cu at (133.7, 110.6)
- added REF**63: Round_Pad_1.7mm_Hole_1.0mm, proto-pcb-pads:RoundPad_1.7mm_Hole_1.0mm, F.Cu at (136.3, 110.6)
- added REF**64: Round_Pad_1.7mm_Hole_1.0mm, proto-pcb-pads:RoundPad_1.7mm_Hole_1.0mm, F.Cu at (138.8, 110.6)
- added REF**65: Round_Pad_1.7mm_Hole_1.0mm, proto-pcb-pads:RoundPad_1.7mm_Hole_1.0mm, F.Cu at (141.3, 110.6)
- added REF**66: Round_Pad_1.7mm_Hole_1.0mm, proto-pcb-pads:RoundPad_1.7mm_Hole_1.0mm, F.Cu at (110.9, 110.6)
- added REF**67: Round_Pad_1.7mm_Hole_1.0mm, proto-pcb-pads:RoundPad_1.7mm_Hole_1.0mm, F.Cu at (108.3, 110.6)
- added REF**68, REF**72: Round_Pad_1.7mm_Hole_1.0mm, proto-pcb-pads:RoundPad_1.7mm_Hole_1.0mm, F.Cu at (113.4, 113.2)
- added REF**69: Round_Pad_1.7mm_Hole_1.0mm, proto-pcb-pads:RoundPad_1.7mm_Hole_1.0mm, F.Cu at (151.5, 110.6)
- added REF**7: Pad_Link_1.7mm_Width_1.0mm, proto-pcb-silks:PadLink_1.7mm_Width_1.0mm, B.Cu at (123.6, 123.3)
- added REF**70: Round_Pad_1.7mm_Hole_1.0mm, proto-pcb-pads:RoundPad_1.7mm_Hole_1.0mm, F.Cu at (110.9, 113.2)
- added REF**71: Round_Pad_1.7mm_Hole_1.0mm, proto-pcb-pads:RoundPad_1.7mm_Hole_1.0mm, F.Cu at (108.3, 113.2)
- added REF**73: Round_Pad_1.7mm_Hole_1.0mm, proto-pcb-pads:RoundPad_1.7mm_Hole_1.0mm, F.Cu at (115.9, 113.2)
- added REF**74: Round_Pad_1.7mm_Hole_1.0mm, proto-pcb-pads:RoundPad_1.7mm_Hole_1.0mm, F.Cu at (118.5, 113.2)
- added REF**75: Round_Pad_1.7mm_Hole_1.0mm, proto-pcb-pads:RoundPad_1.7mm_Hole_1.0mm, F.Cu at (121.0, 113.2)
- added REF**76: Round_Pad_1.7mm_Hole_1.0mm, proto-pcb-pads:RoundPad_1.7mm_Hole_1.0mm, F.Cu at (123.6, 113.2)
- added REF**77: Round_Pad_1.7mm_Hole_1.0mm, proto-pcb-pads:RoundPad_1.7mm_Hole_1.0mm, F.Cu at (126.1, 113.2)
- added REF**78: Round_Pad_1.7mm_Hole_1.0mm, proto-pcb-pads:RoundPad_1.7mm_Hole_1.0mm, F.Cu at (128.6, 113.2)
- added REF**79: Round_Pad_1.7mm_Hole_1.0mm, proto-pcb-pads:RoundPad_1.7mm_Hole_1.0mm, F.Cu at (131.2, 113.2)
- added REF**8: Pad_Link_1.7mm_Width_1.0mm, proto-pcb-silks:PadLink_1.7mm_Width_1.0mm, B.Cu at (126.1, 123.3)
- added REF**80: Round_Pad_1.7mm_Hole_1.0mm, proto-pcb-pads:RoundPad_1.7mm_Hole_1.0mm, F.Cu at (133.7, 113.2)
- added REF**81: Round_Pad_1.7mm_Hole_1.0mm, proto-pcb-pads:RoundPad_1.7mm_Hole_1.0mm, F.Cu at (136.3, 113.2)
- added REF**82: Round_Pad_1.7mm_Hole_1.0mm, proto-pcb-pads:RoundPad_1.7mm_Hole_1.0mm, F.Cu at (138.8, 113.2)
- added REF**83: Round_Pad_1.7mm_Hole_1.0mm, proto-pcb-pads:RoundPad_1.7mm_Hole_1.0mm, F.Cu at (141.3, 113.2)
- added REF**84, REF**90: Round_Pad_1.7mm_Hole_1.0mm, proto-pcb-pads:RoundPad_1.7mm_Hole_1.0mm, F.Cu at (113.4, 115.7)
- added REF**85: Round_Pad_1.7mm_Hole_1.0mm, proto-pcb-pads:RoundPad_1.7mm_Hole_1.0mm, F.Cu at (110.9, 115.7)
- added REF**86: Round_Pad_1.7mm_Hole_1.0mm, proto-pcb-pads:RoundPad_1.7mm_Hole_1.0mm, F.Cu at (108.3, 115.7)
- added REF**88: Round_Pad_1.7mm_Hole_1.0mm, proto-pcb-pads:RoundPad_1.7mm_Hole_1.0mm, F.Cu at (110.9, 118.2)
- added REF**89: Round_Pad_1.7mm_Hole_1.0mm, proto-pcb-pads:RoundPad_1.7mm_Hole_1.0mm, F.Cu at (108.3, 118.2)
- added REF**9: Pad_Link_1.7mm_Width_1.0mm, proto-pcb-silks:PadLink_1.7mm_Width_1.0mm, B.Cu at (133.7, 123.3)
- added REF**9: Pad_Link_1.7mm_Width_1.0mm, proto-pcb-silks:PadLink_1.7mm_Width_1.0mm, B.Cu at (128.6, 123.3)
- added REF**91: Round_Pad_1.7mm_Hole_1.0mm, proto-pcb-pads:RoundPad_1.7mm_Hole_1.0mm, F.Cu at (115.9, 115.7)
- added REF**92: Round_Pad_1.7mm_Hole_1.0mm, proto-pcb-pads:RoundPad_1.7mm_Hole_1.0mm, F.Cu at (118.5, 115.7)
- added REF**93: Round_Pad_1.7mm_Hole_1.0mm, proto-pcb-pads:RoundPad_1.7mm_Hole_1.0mm, F.Cu at (121.0, 115.7)
- added REF**94: Round_Pad_1.7mm_Hole_1.0mm, proto-pcb-pads:RoundPad_1.7mm_Hole_1.0mm, F.Cu at (123.6, 115.7)
- added REF**95: Round_Pad_1.7mm_Hole_1.0mm, proto-pcb-pads:RoundPad_1.7mm_Hole_1.0mm, F.Cu at (126.1, 115.7)
- added REF**96: Round_Pad_1.7mm_Hole_1.0mm, proto-pcb-pads:RoundPad_1.7mm_Hole_1.0mm, F.Cu at (128.6, 115.7)
- added REF**97: Round_Pad_1.7mm_Hole_1.0mm, proto-pcb-pads:RoundPad_1.7mm_Hole_1.0mm, F.Cu at (131.2, 115.7)
- added REF**98: Round_Pad_1.7mm_Hole_1.0mm, proto-pcb-pads:RoundPad_1.7mm_Hole_1.0mm, F.Cu at (133.7, 115.7)
- added REF**99: Round_Pad_1.7mm_Hole_1.0mm, proto-pcb-pads:RoundPad_1.7mm_Hole_1.0mm, F.Cu at (136.3, 115.7)
- moved J1 0.75 mm to (104.3, 119.2)
- moved J2 0.75 mm to (104.3, 103.4)
- moved J3 0.05 mm to (157.4, 110.0)
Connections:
- J1 pad 1: GND -> unconnected-(J1-Pad1)
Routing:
- net (no net): track 0.00 -> 467.4 mm
- net GND: track 52.6 -> 0.00 mm
- net J1-PIN5: track 0.00 -> 31.9 mm
- net J2-PIN1: track 0.00 -> 26.0 mm
- net J1-PIN1: track 0.00 -> 18.4 mm
- net J2-PIN3: track 0.00 -> 17.8 mm
- net J1-PIN2: track 0.00 -> 17.7 mm
- net J2-PIN5: track 0.00 -> 17.1 mm
- net J1-PIN3: track 0.00 -> 16.1 mm
- net J1-PIN4: track 0.00 -> 15.9 mm
- net J1-PIN6: track 0.00 -> 15.8 mm
- net J2-PIN4: track 0.00 -> 15.0 mm
- net J2-PIN2: track 0.00 -> 14.8 mm
- net J2-PIN6: track 0.00 -> 14.8 mm
- net J3-PIN3: track 0.00 -> 14.4 mm
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- removed copper zone on F.Cu, net GND
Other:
- board text added: "1"
- board text added: "2"
- board text added: "3"
- board text added: "4"
- board text added: "5"
- board text added: "6"
